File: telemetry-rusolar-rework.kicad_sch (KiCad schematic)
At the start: 85 parts, among them IC3 USBLC6-2P6, J1 USART Debug, J10 JP, J11 USB_B_Micro, J12 I2C, J13 GR2, J14 GR1, J16 47219-2001, J18 SWD, J2 SPI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

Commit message: Added temp
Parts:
- R20, R22, R23: value 47k -> 100k
- R21: value 47k -> 90k

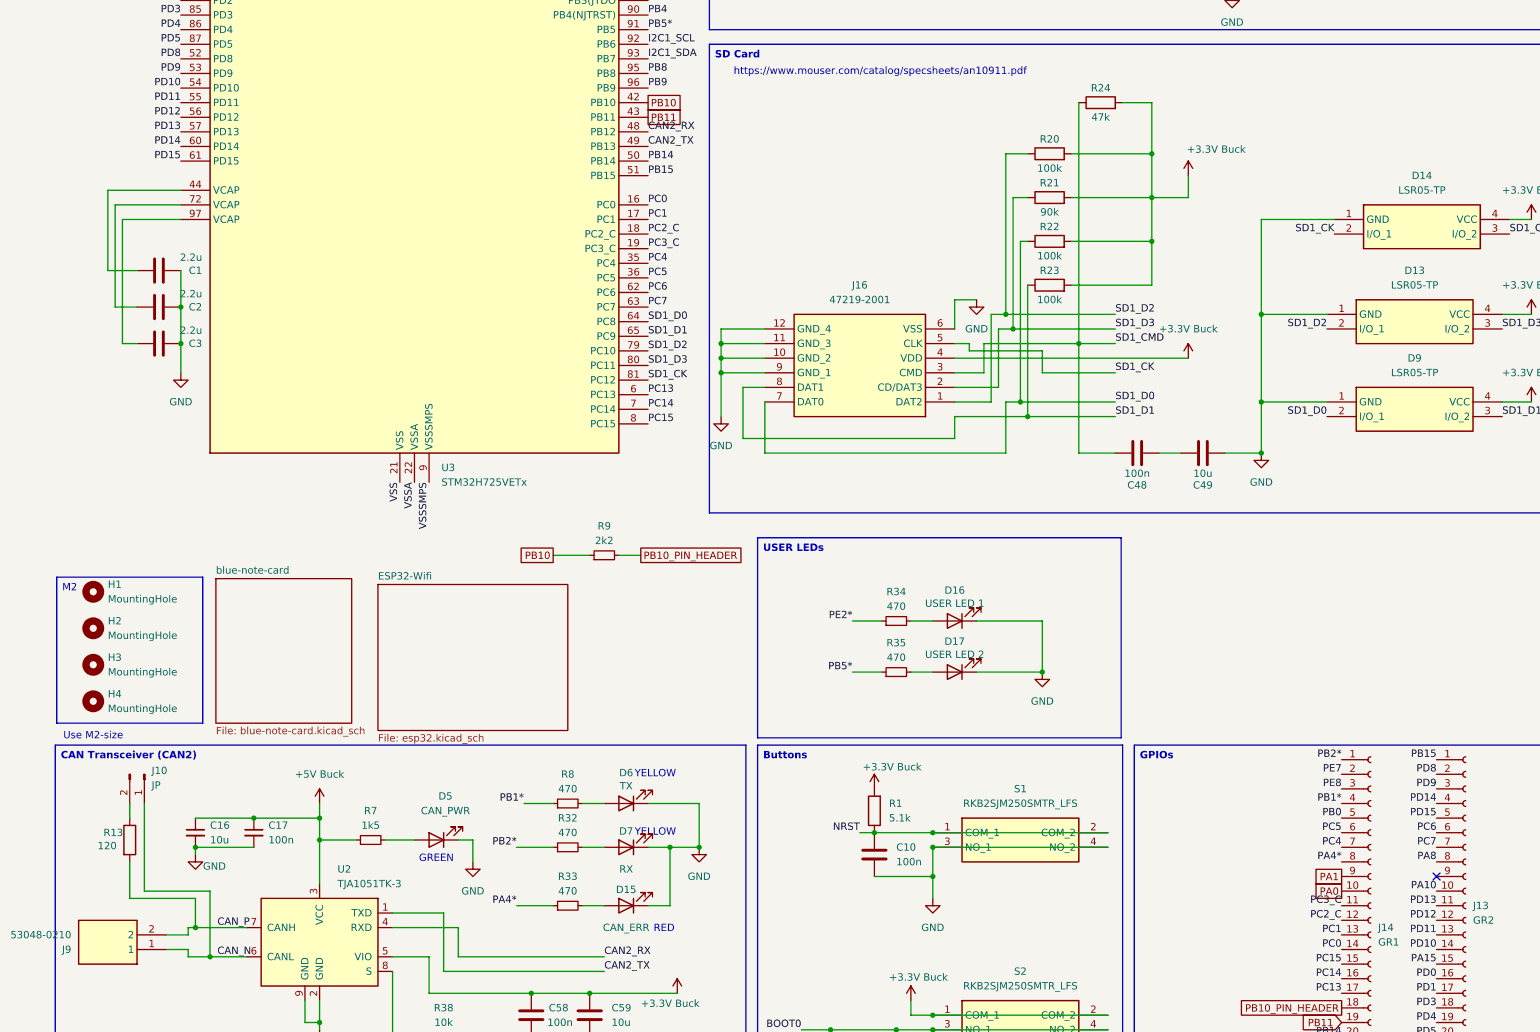
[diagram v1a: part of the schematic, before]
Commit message: Added AUX_EN, I2C com to Blues, LED labels
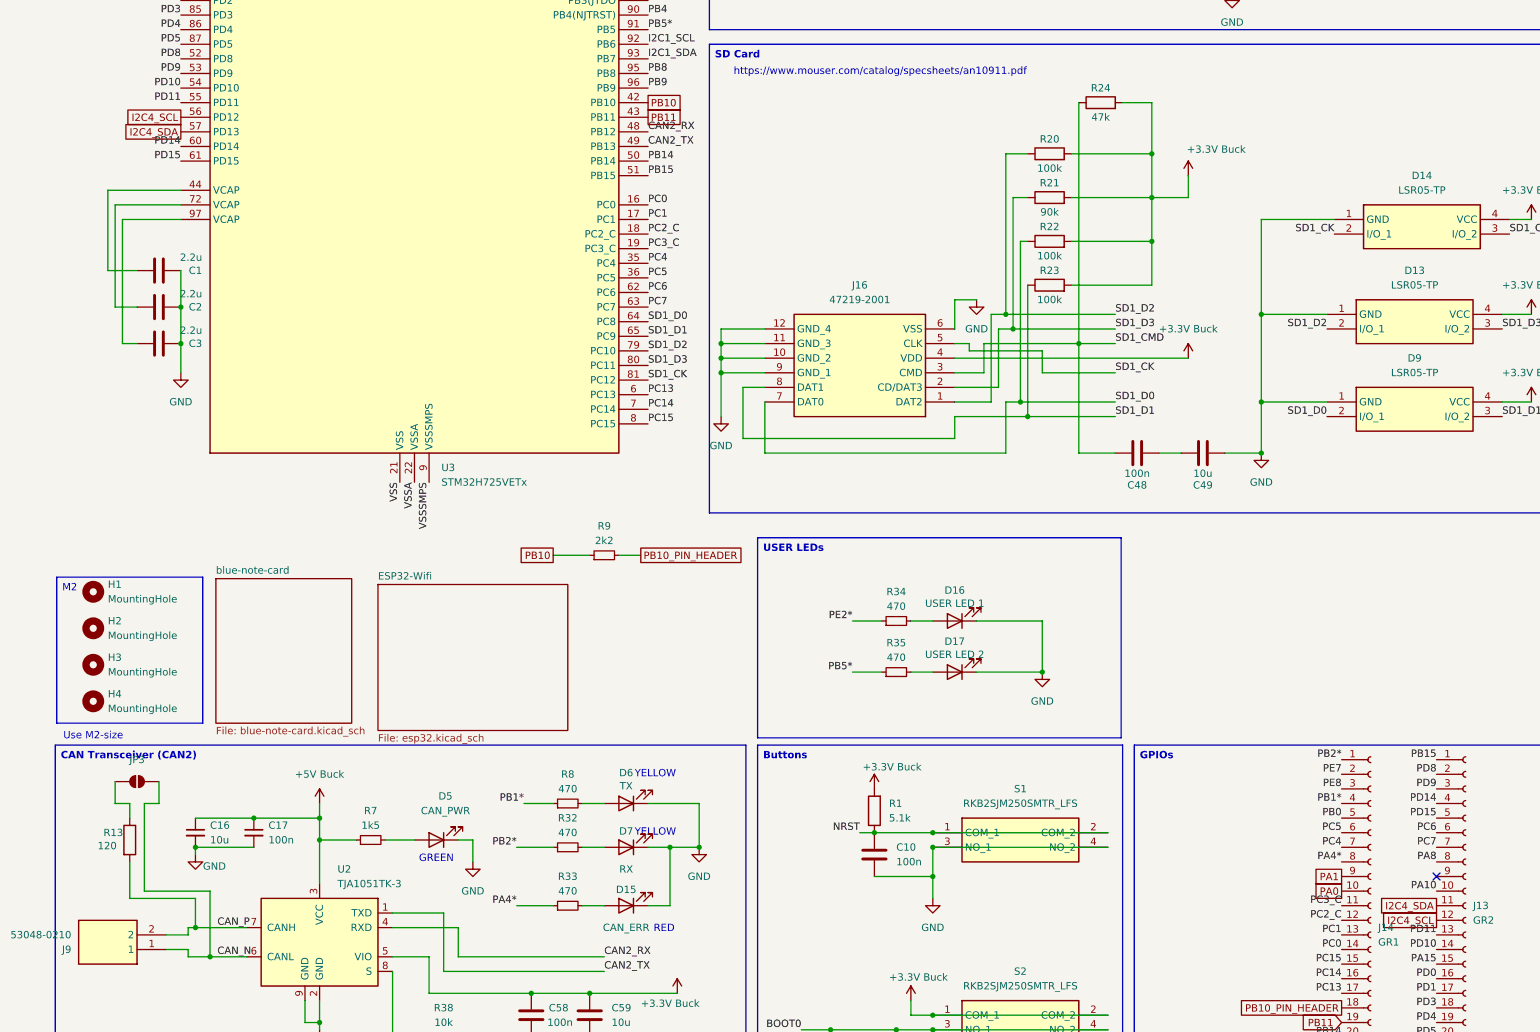
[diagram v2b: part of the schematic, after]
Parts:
- removed J10: JP, Connector_PinHeader_2.00mm:PinHeader_1x02_P2.00mm_Vertical, symbol Connector:Conn_01x02_Pin
- added JP3: SolderJumper_2_Open, Jumper:SolderJumper-2_P1.3mm_Open_RoundedPad1.0x1.5mm, symbol Jumper:SolderJumper_2_Open
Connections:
- net CAN_N: now also JP3.2 (B)
- net at R13.1: now also JP3.1 (A)
- net PD12 renamed I2C4_SCL
- net PD13 renamed I2C4_SDA

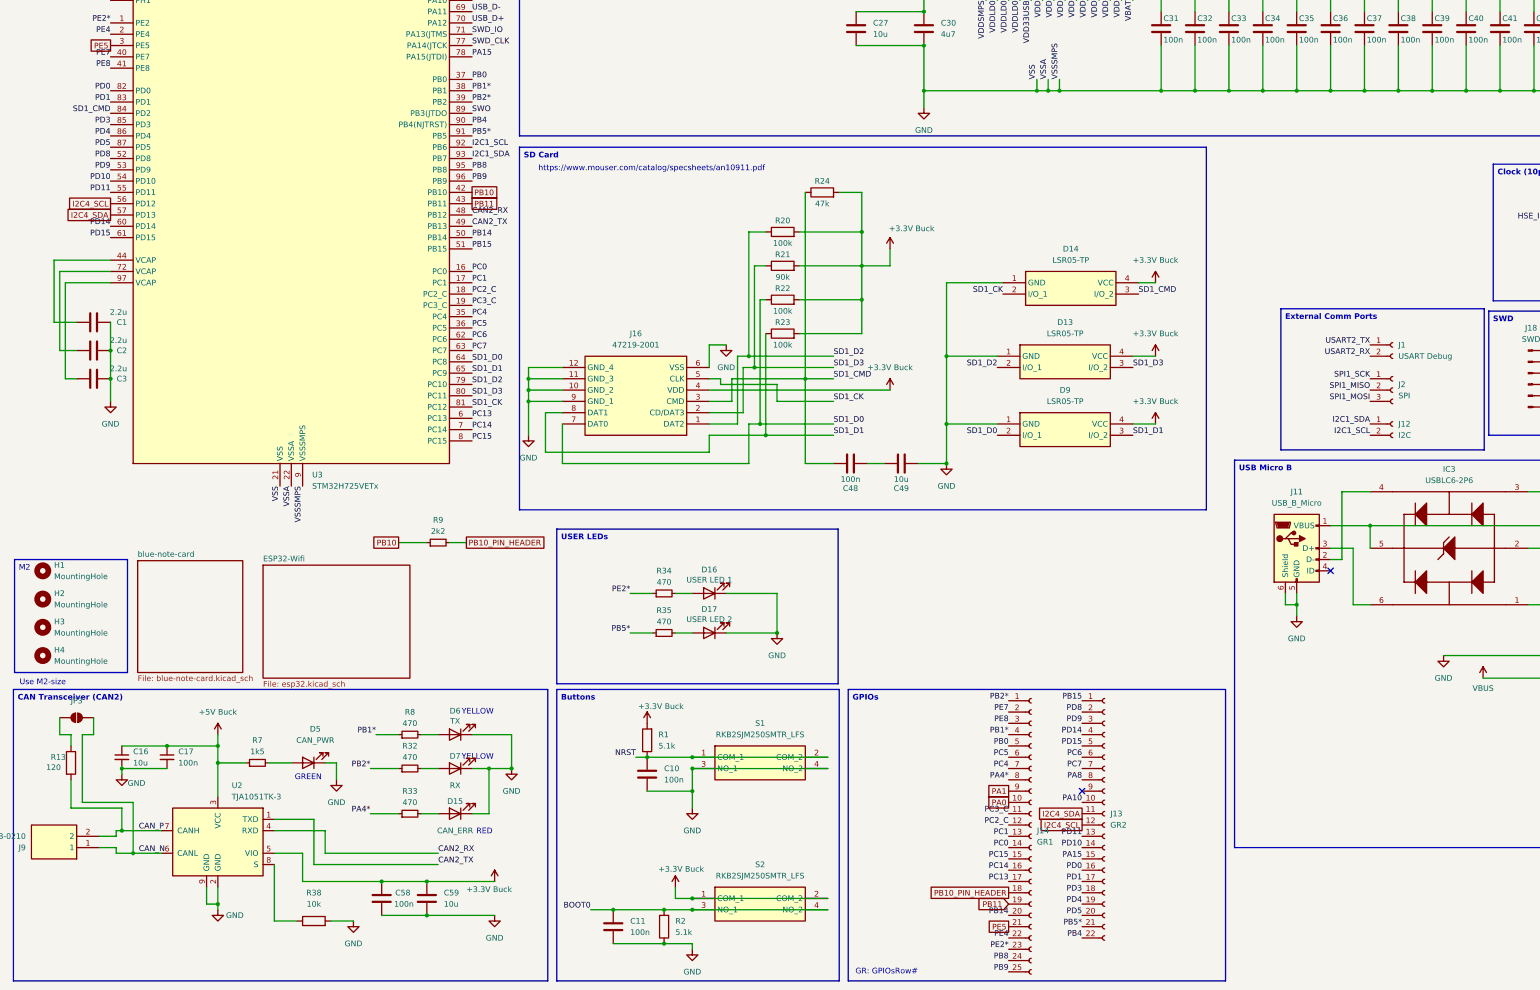
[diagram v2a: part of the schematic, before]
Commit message: Added module LEDs, I2C for Blues Com
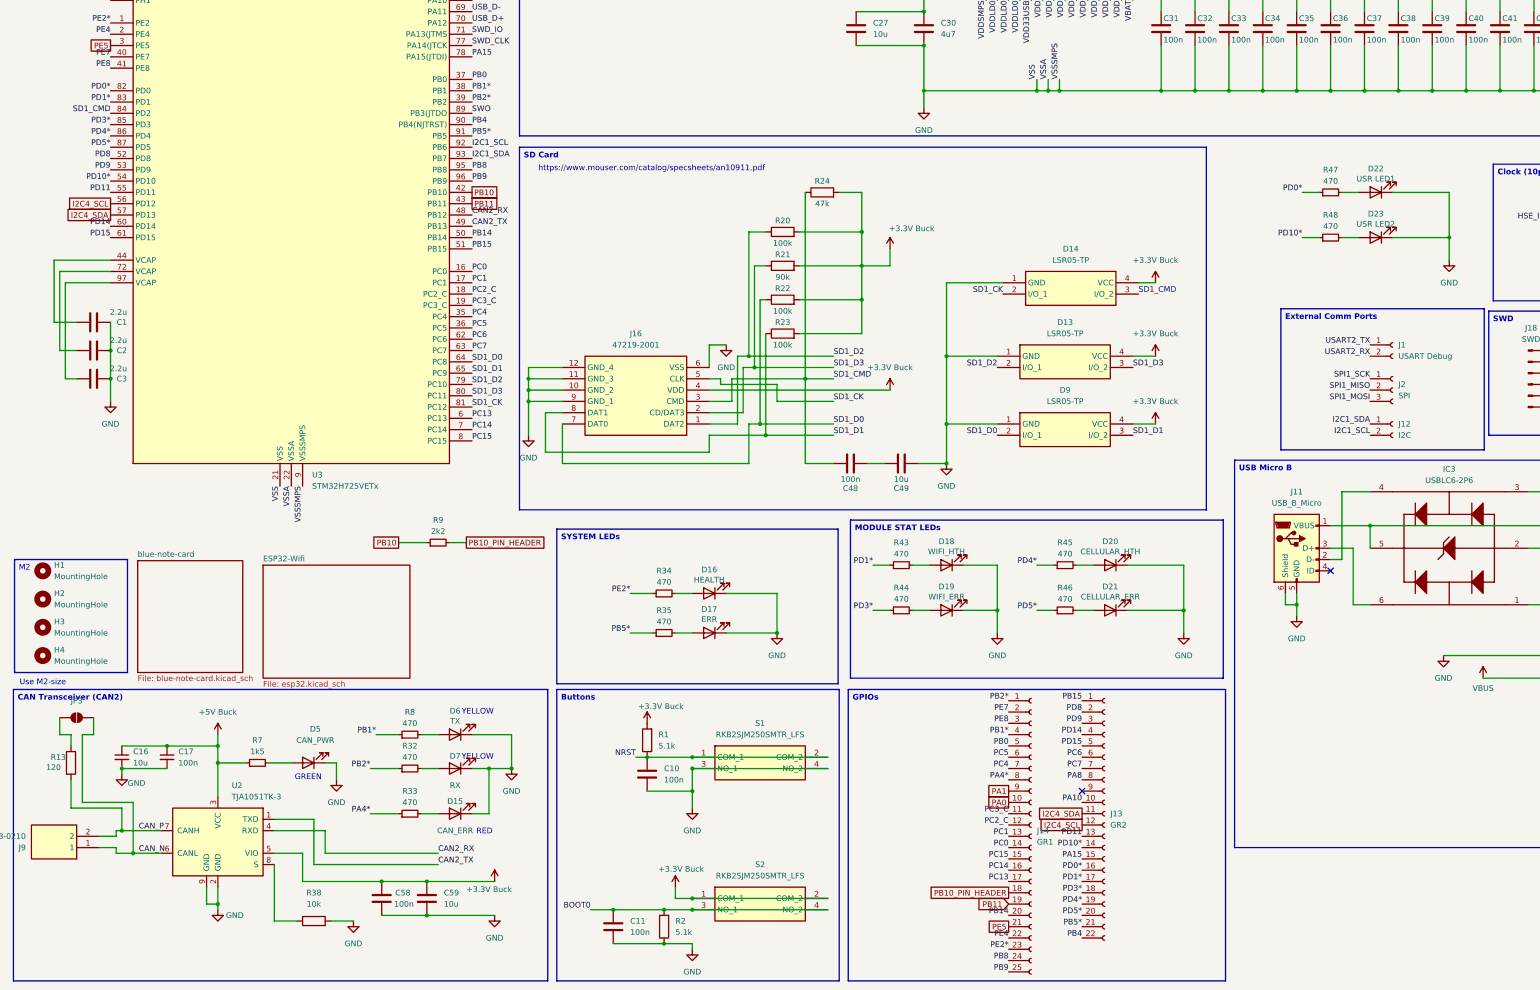
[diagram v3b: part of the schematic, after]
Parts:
- added D18: WIFI_HTH, LED_SMD:LED_0805_2012Metric_Pad1.15x1.40mm_HandSolder, symbol Device:LED
- added D19: WIFI_ERR, LED_SMD:LED_0805_2012Metric_Pad1.15x1.40mm_HandSolder, symbol Device:LED
- added D20: CELLULAR_HTH, LED_SMD:LED_0805_2012Metric_Pad1.15x1.40mm_HandSolder, symbol Device:LED
- added D21: CELLULAR_ERR, LED_SMD:LED_0805_2012Metric_Pad1.15x1.40mm_HandSolder, symbol Device:LED
- added D22: USR LED1, LED_SMD:LED_0805_2012Metric_Pad1.15x1.40mm_HandSolder, symbol Device:LED
- added D23: USR LED2, LED_SMD:LED_0805_2012Metric_Pad1.15x1.40mm_HandSolder, symbol Device:LED
- added R43, R44, R45, R46, R47, R48: 470, Resistor_SMD:R_0603_1608Metric_Pad0.98x0.95mm_HandSolder, symbol Device:R_Small
- D16: value USER LED 1 -> HEALTH
- D17: value USER LED 2 -> ERR
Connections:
- net GND: now also D18.1 (K), D19.1 (K), D20.1 (K), D21.1 (K), D22.1 (K), D23.1 (K)
- net PD0 renamed PD0*
- net PD0*: now also R47.1
- net PD1 renamed PD1*
- net PD1*: now also R43.1
- net PD10 renamed PD10*
- net PD10*: now also R48.1
- net PD3 renamed PD3*
- net PD3*: now also R44.1
- net PD4 renamed PD4*
- net PD4*: now also R45.1
- net PD5 renamed PD5*
- net PD5*: now also R46.1
- new net: D20.2 (A), R45.2
- new net: D18.2 (A), R43.2
- new net: D19.2 (A), R44.2
- new net: D21.2 (A), R46.2
- new net: D22.2 (A), R47.2
- new net: D23.2 (A), R48.2
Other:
- note removed: "GR: GPIOsRow#"

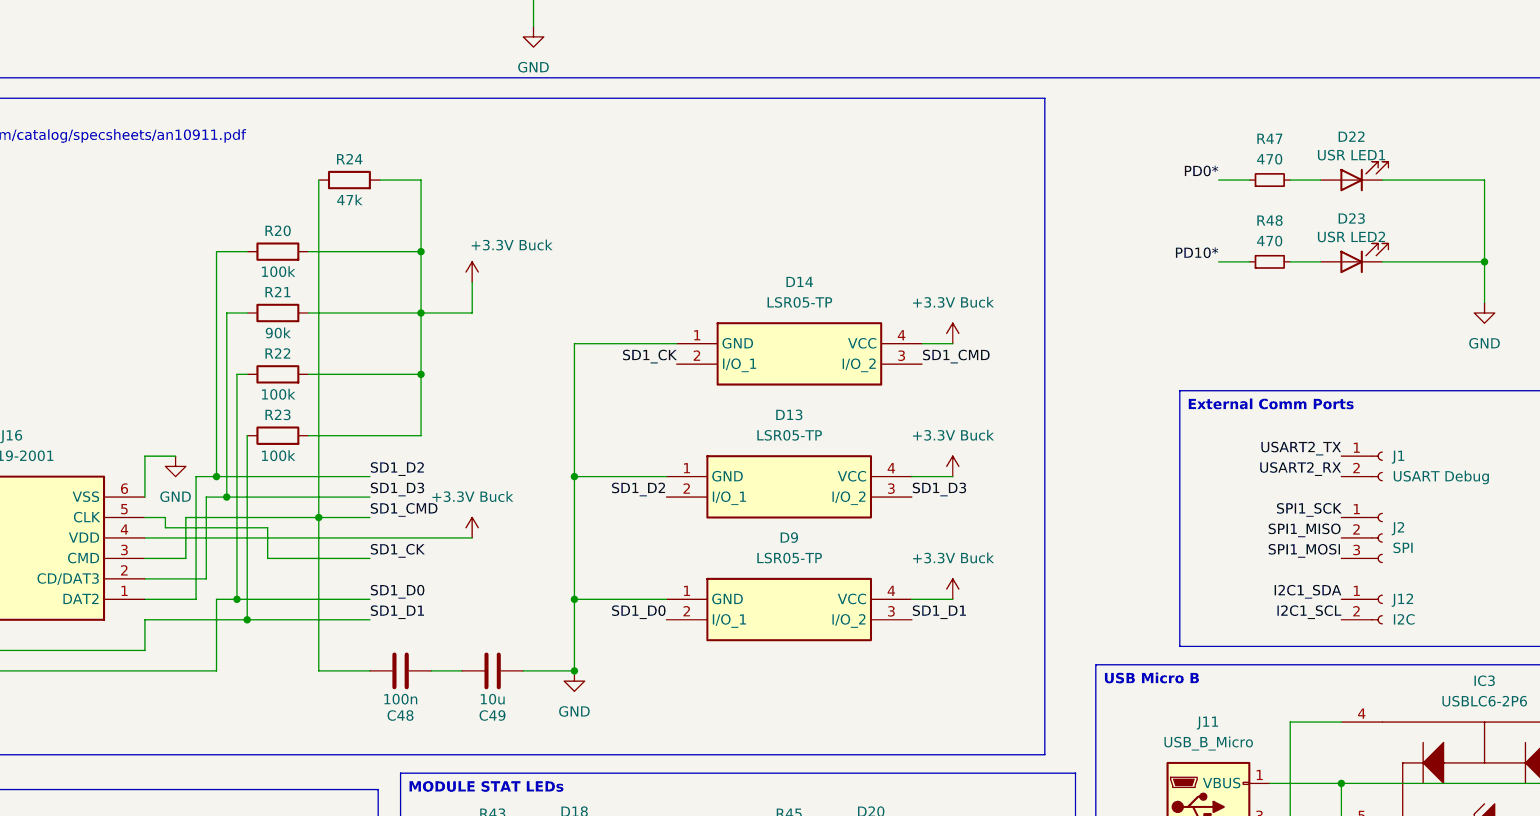
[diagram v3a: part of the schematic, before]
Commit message: Fixed SD Card layout
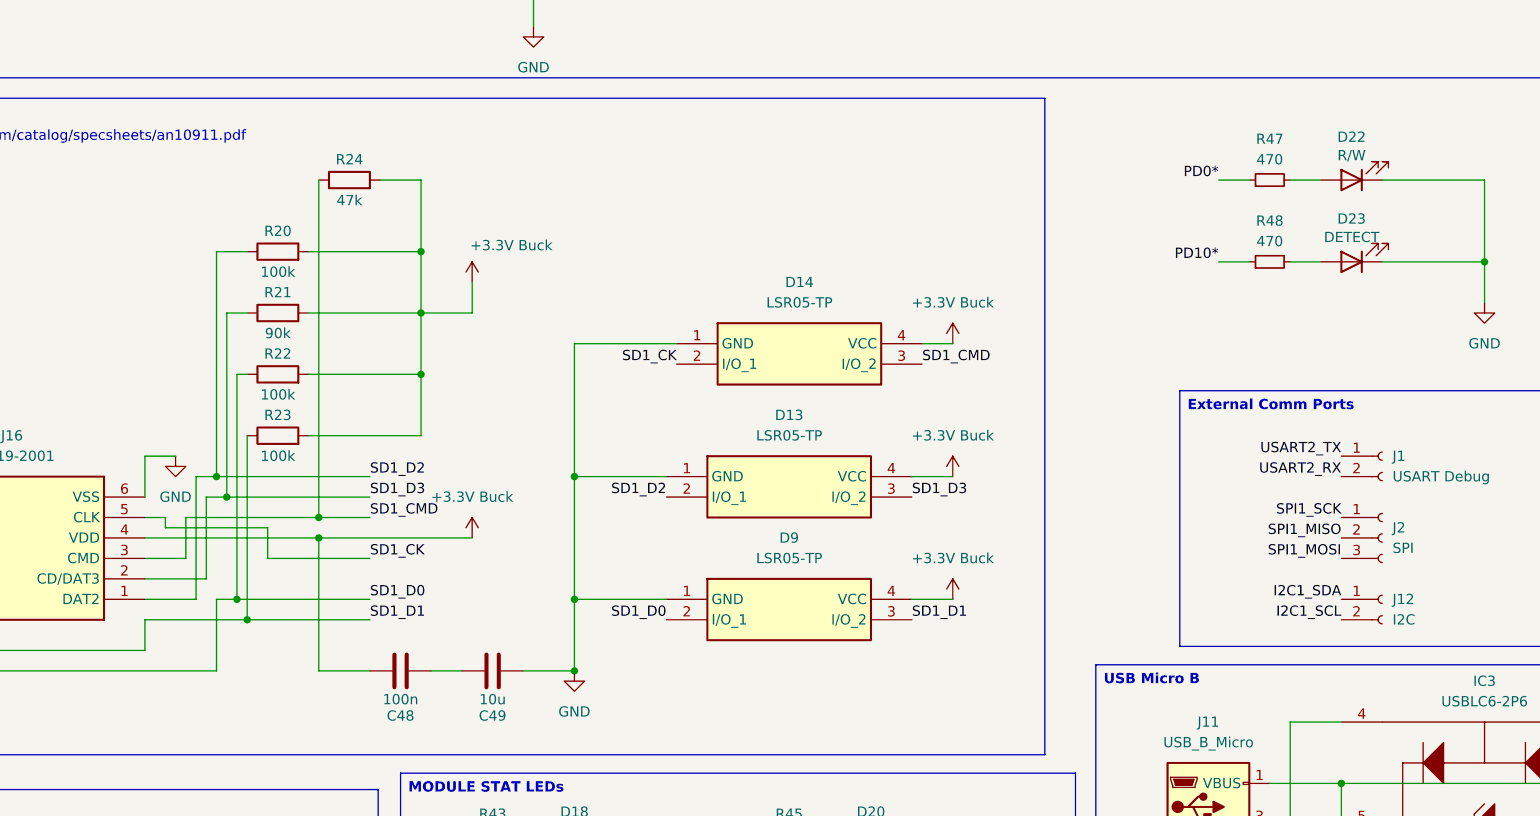
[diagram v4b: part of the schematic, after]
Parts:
- D22: value USR LED1 -> R/W
- D23: value USR LED2 -> DETECT
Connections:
- net +3.3V Buck: now also C48.1
- net SD1_CMD: no longer C48.1
